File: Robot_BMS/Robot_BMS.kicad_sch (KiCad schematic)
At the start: 15 parts, among them IC1 BQ34Z100PWR-R2, IC2 STUSB4710AQTR, J1 USB_C_Receptacle_PowerOnly_24P, U1 BQ297xy, U2 BQ297xy, U3 BQ297xy, U4 MCP73833-xxx-MF, U5 MCP73833-xxx-MF, U6 MCP73833-xxx-MF

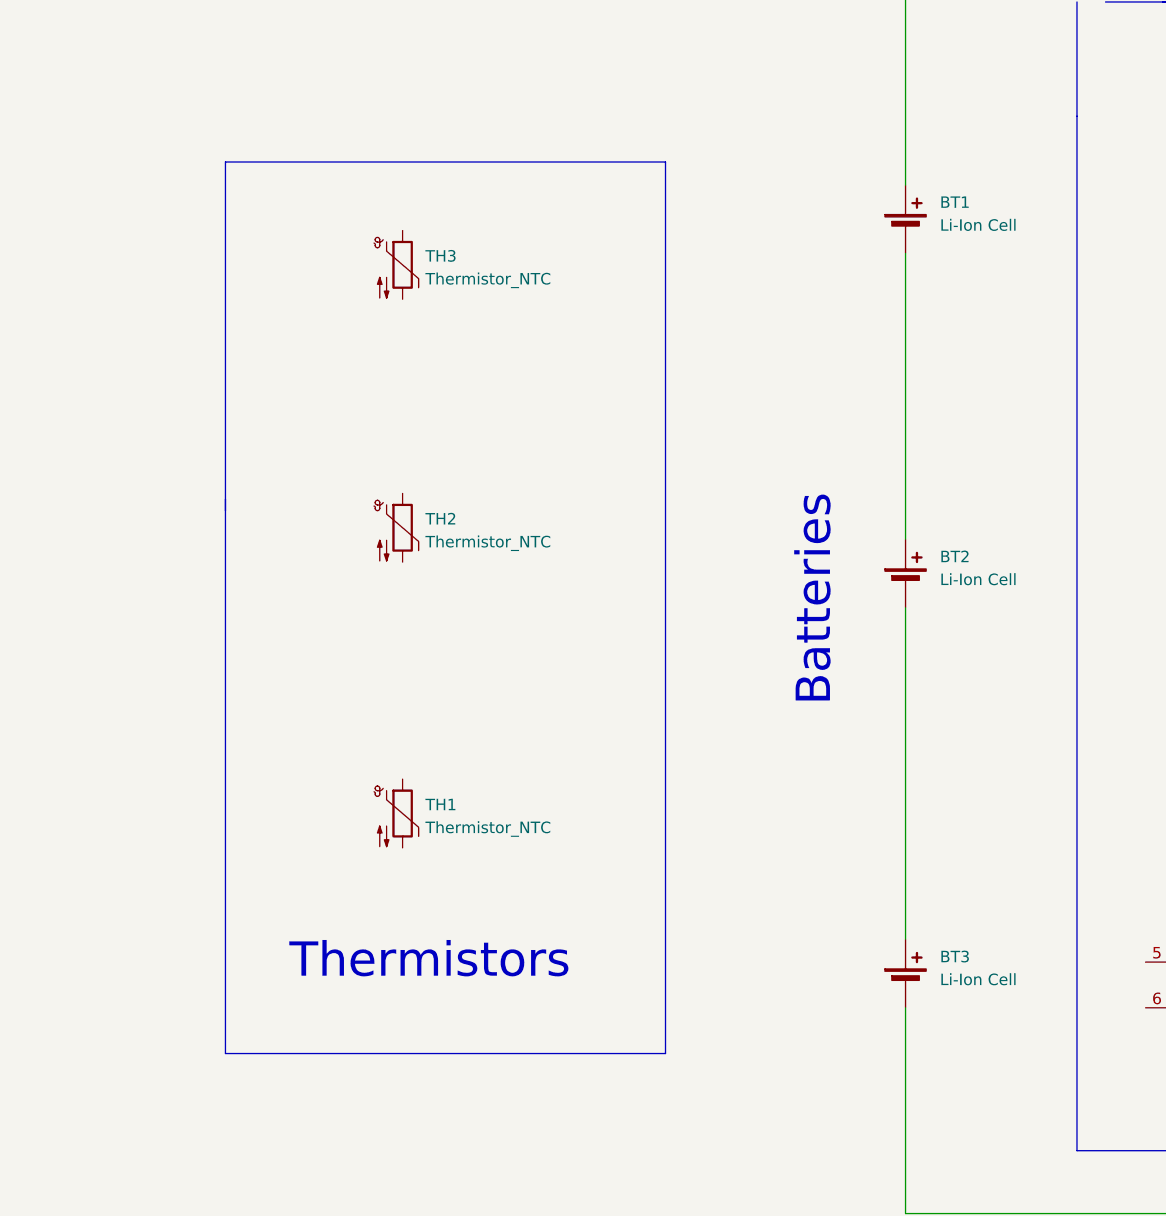
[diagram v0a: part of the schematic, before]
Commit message: NTC's implemented
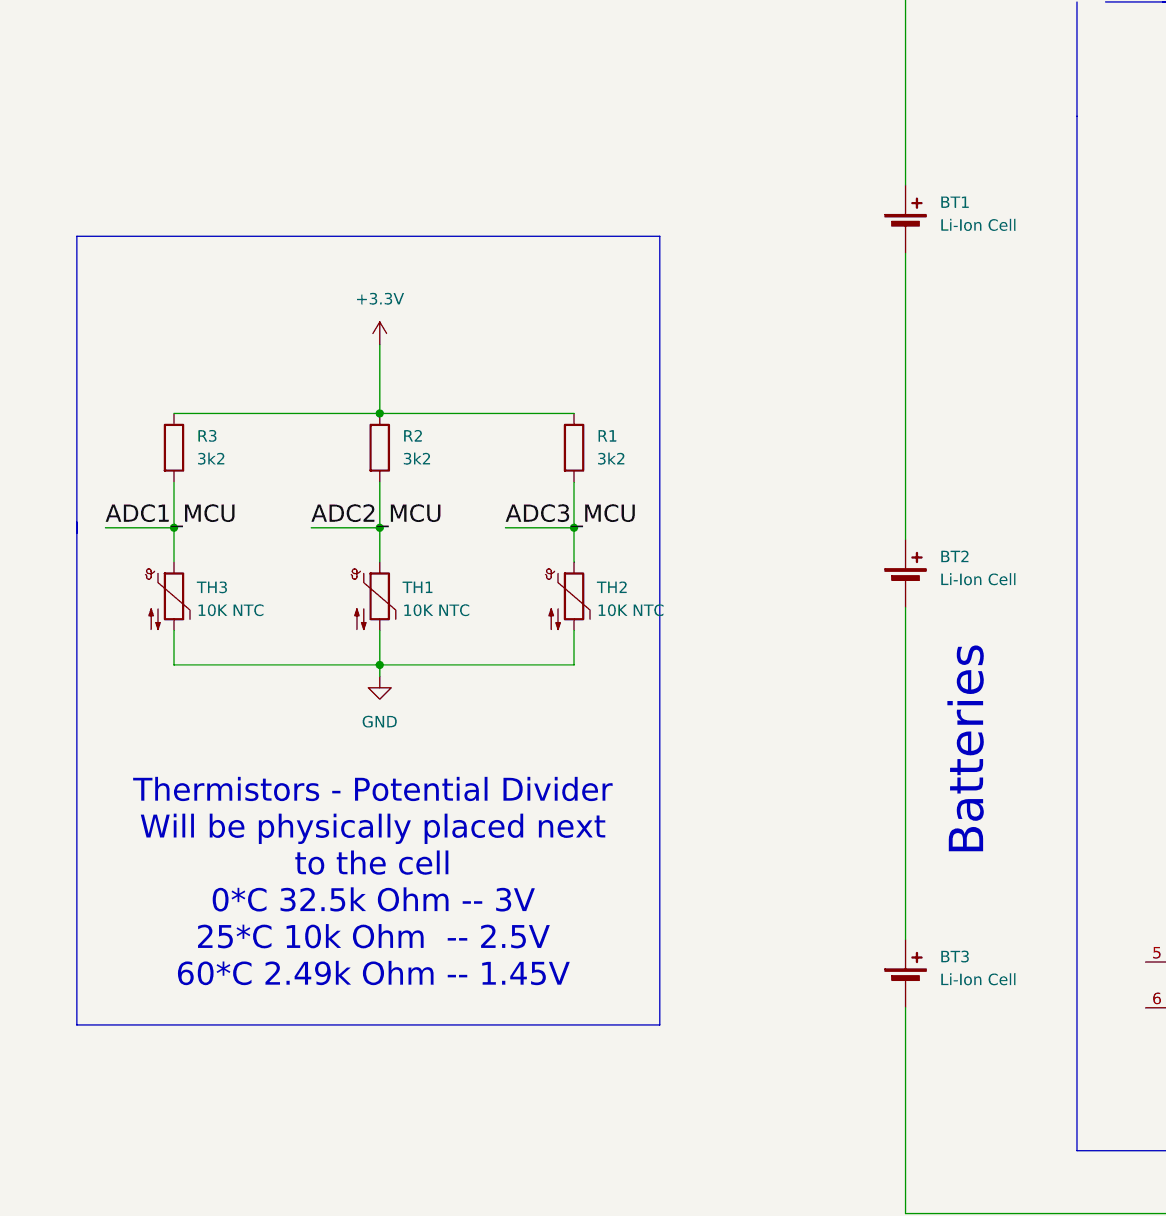
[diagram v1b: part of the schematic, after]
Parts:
- added R1, R2, R3: 3k2, symbol Device:R
- TH1, TH2, TH3: value Thermistor_NTC -> 10K NTC
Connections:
- net ADC3_MCU: now reaches TH2.1
- net ADC3_MCU: now also R1.2
- net GND: now reaches TH2.2
- net GND: now also TH1.2, TH3.2
- net ADC1_MCU: now reaches TH3.1
- net ADC1_MCU: now also R3.2
- net ADC2_MCU: now reaches TH1.1
- net ADC2_MCU: now also R2.2
- new net +3.3V: R1.1, R2.1, R3.1
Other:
- note added: "Thermistors - Potential Divider Will be physically placed next to the cell 0*C 32.5k Ohm -- 3V 25*C 10k Ohm -- 2.5V 60*C 2.49k Ohm -- 1.45V"
- note removed: "Thermistors"
- moved on the sheet: TH3

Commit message: Battery Protection IC implemented, N Channel Fet selected
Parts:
- added C1, C2, C3: 0.1u, symbol Device:C
- added Q1, Q2, Q3, Q4, Q5, Q6: SIS413DN-T1-GE3, SIS862DNT1GE3, symbol SIS413DN-T1-GE3:SIS413DN-T1-GE3
- added R4, R6, R8: 2k2, symbol Device:R
- added R5, R7, R9: 330, symbol Device:R
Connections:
- net at BT1.1 (+): now also R5.1
- net at BT1.2 (-), BT2.1 (+): now also Q2.1 (S_1), Q2.2 (S_2), Q2.3 (S_3), R7.1
- net at U2.2 (Cout): now also Q3.4 (G)
- net at U2.3 (Dout): now also Q4.4 (G)
- net at U2.4 (VSS): now also C2.2, Q4.5 (D_1), Q4.6 (D_2), Q4.7 (D_3), Q4.8 (D_4), R6.1
- net at U2.5 (BAT): now also C2.1, R7.2
- net at U2.6 (V-): now also R6.2
- net at BT2.2 (-), BT3.1 (+): now also Q3.1 (S_1), Q3.2 (S_2), Q3.3 (S_3), R9.1
- net at BT3.2 (-): now also Q5.1 (S_1), Q5.2 (S_2), Q5.3 (S_3)
- net at U1.2 (Cout): now also Q2.4 (G)
- net at U1.3 (Dout): now also Q1.4 (G)
- net at U1.4 (VSS): now also C1.2, Q1.5 (D_1), Q1.6 (D_2), Q1.7 (D_3), Q1.8 (D_4), R4.1
- net at U1.5 (BAT): now also C1.1, R5.2
- net at U1.6 (V-): now also R4.2
- net at U3.2 (Cout): now also Q5.4 (G)
- net at U3.3 (Dout): now also Q6.4 (G)
- net at U3.4 (VSS): now also C3.2, Q6.5 (D_1), Q6.6 (D_2), Q6.7 (D_3), Q6.8 (D_4), R8.1
- net at U3.5 (BAT): now also C3.1, R9.2
- net at U3.6 (V-): now also R8.2
- new net: Q5.5 (D_1), Q5.6 (D_2), Q5.7 (D_3), Q5.8 (D_4), Q6.1 (S_1), Q6.2 (S_2), Q6.3 (S_3)
- new net: Q1.1 (S_1), Q1.2 (S_2), Q1.3 (S_3), Q2.5 (D_1), Q2.6 (D_2), Q2.7 (D_3), Q2.8 (D_4)
- new net: Q3.5 (D_1), Q3.6 (D_2), Q3.7 (D_3), Q3.8 (D_4), Q4.1 (S_1), Q4.2 (S_2), Q4.3 (S_3)
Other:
- note added: "The drain current of the FET determines, charging and discharging current"
- note removed: "Batteries"
- moved on the sheet: BT1, R1, R2, R3, TH1, TH2, TH3, U1

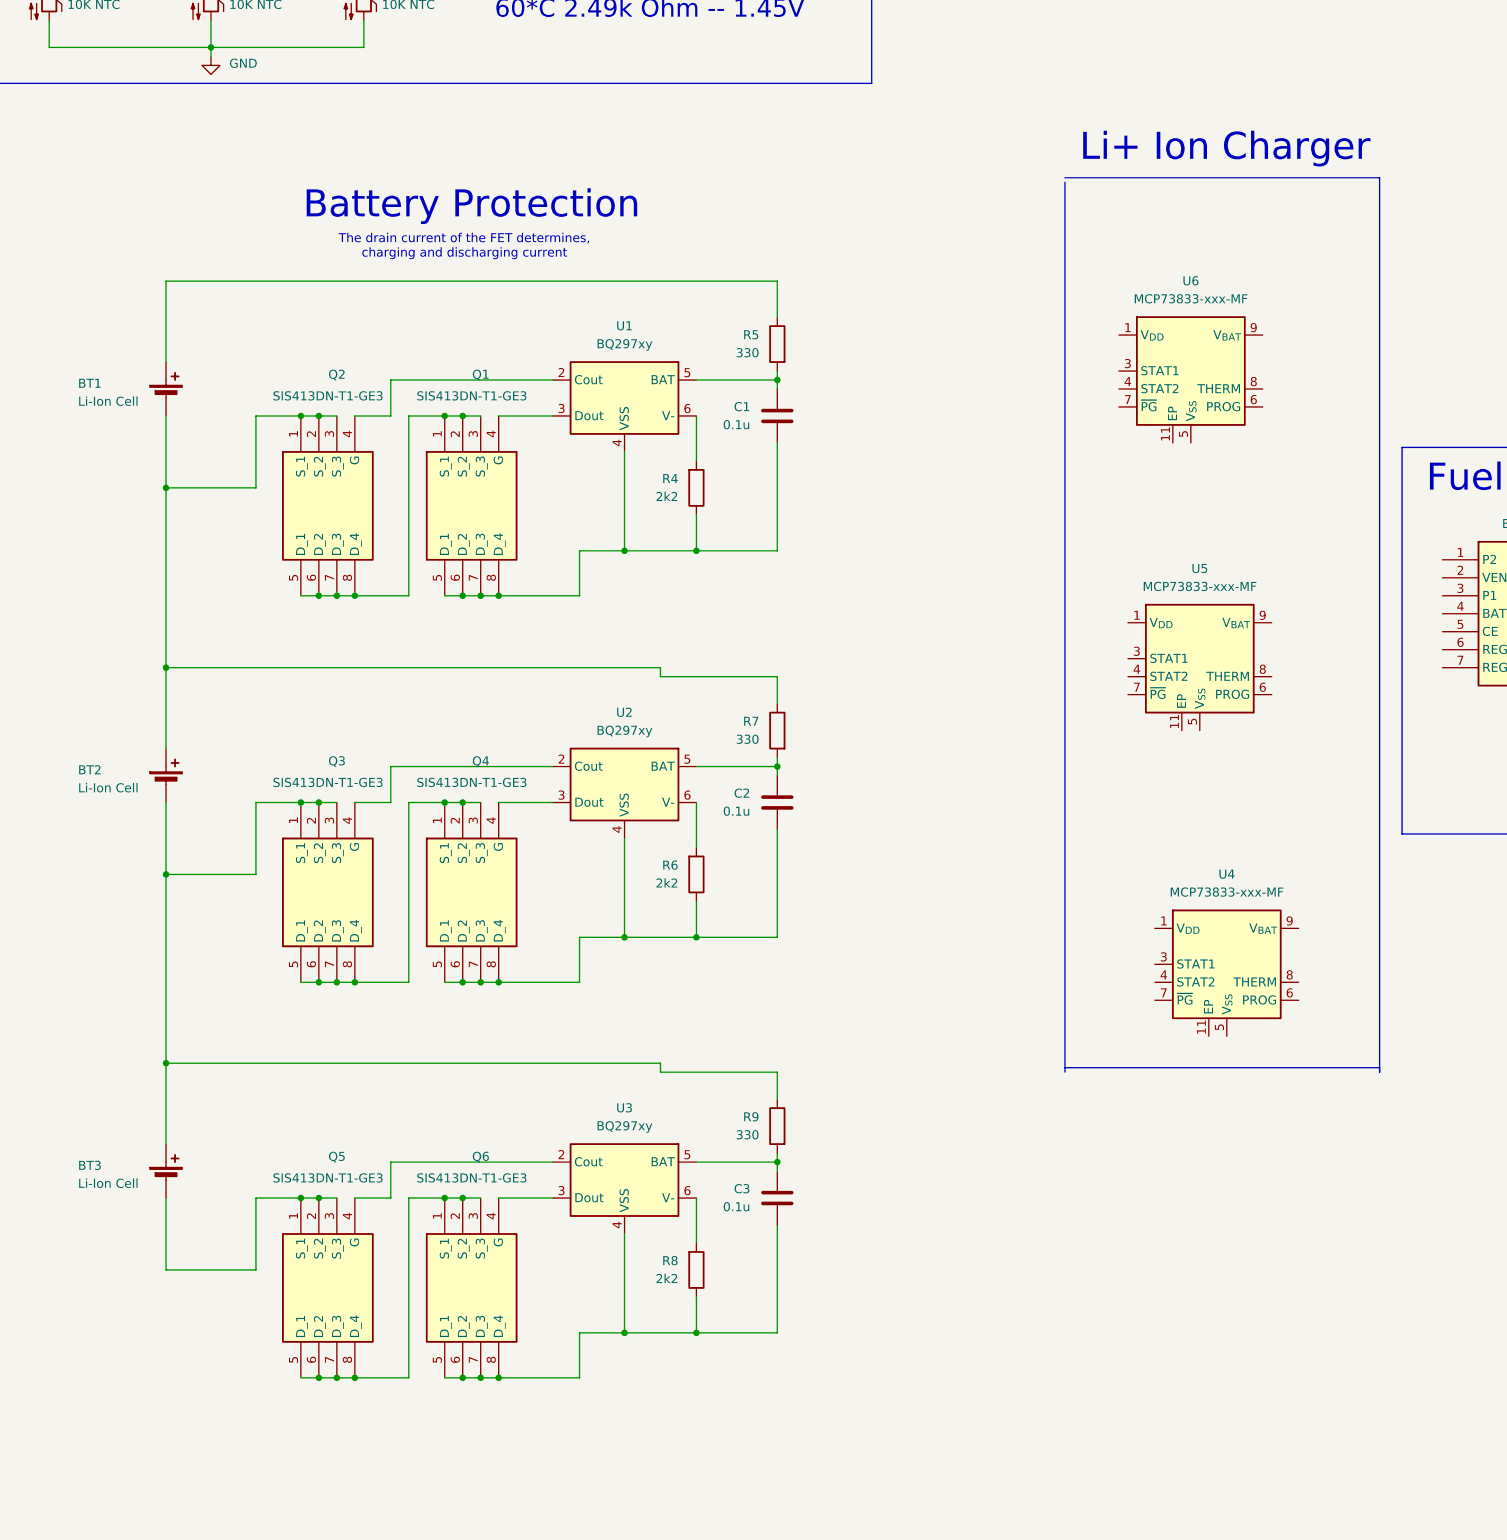
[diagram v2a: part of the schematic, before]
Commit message: comments on Bat Protection IC added
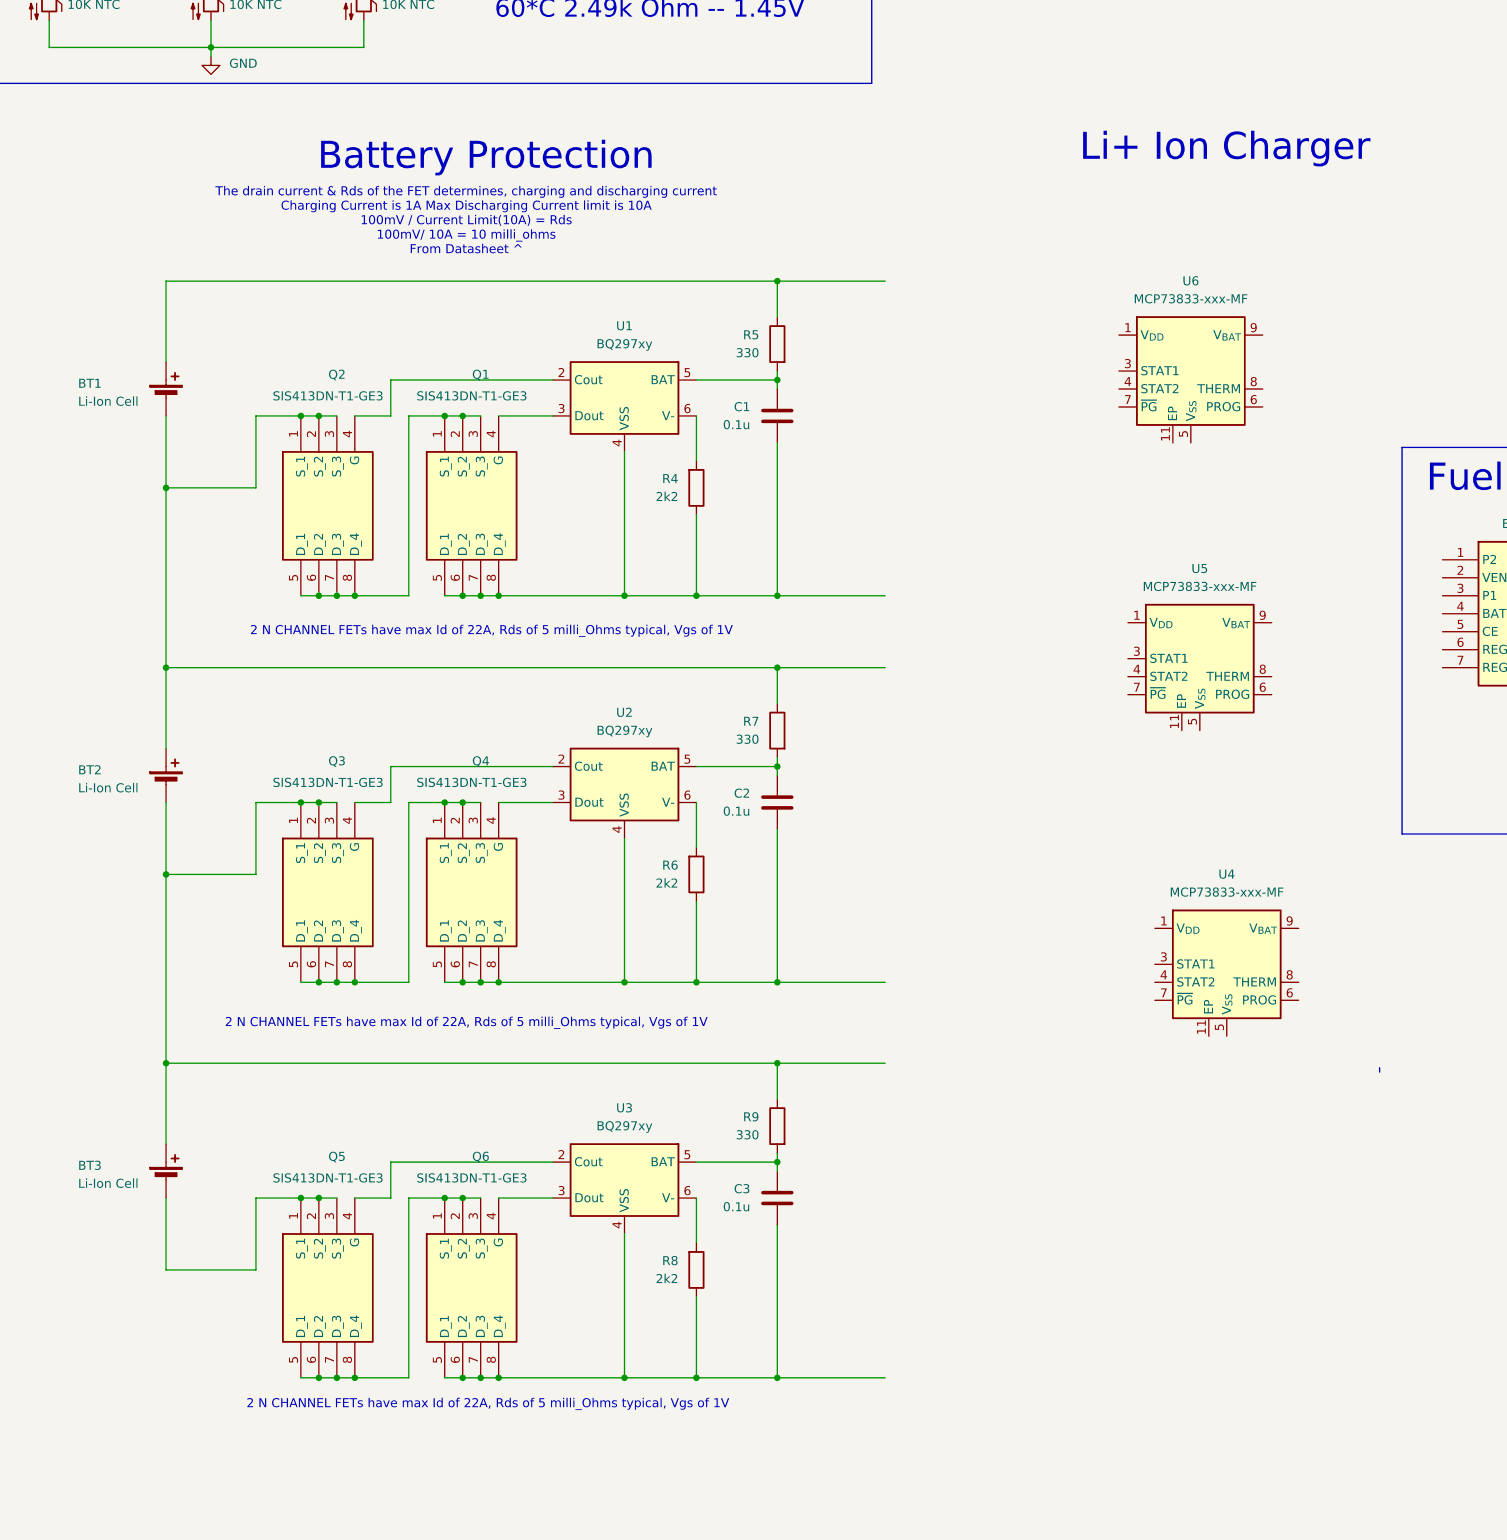
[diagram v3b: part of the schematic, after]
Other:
- note added: "2 N CHANNEL FETs have max Id of 22A, Rds of 5 milli_Ohms typical, Vgs of 1V"
- note added: "The drain current & Rds of the FET determines, charging and discharging current Charging Current is 1A Max Discharging Current limit is 10A 100mV / Current Limit(10A) = Rds 100mV/ 10A = 10 milli_ohms From Datasheet ^"
- note removed: "The drain current of the FET determines, charging and discharging current"

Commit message: Li+ Ion implemented into schematic for one of the cells
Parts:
- removed U4, U5: MCP73833-xxx-MF, Package_DFN_QFN:DFN-10-1EP_3x3mm_P0.5mm_EP1.58x2.35mm, symbol Battery_Management:MCP73833-xxx-MF
- added C4, C5: 10u, symbol Device:C
- added LED1: SML-D12V8WT86, SMLD12V8WT86, symbol SML-D12V8WT86:SML-D12V8WT86
- added LED2: KT_EELP41.12-S2U1-25-2X4X-5-R18, KTEELP4112S2U1252X4X5R18, symbol KT EELP41.12-S2U1-25-2X4X-5-R18:KT_EELP41.12-S2U1-25-2X4X-5-R18
- added LED3: KY_EELP41.22_Q2T1-36-A8J8-020-R18, KYEELP4122Q2T136A8J8020R18, symbol KY EELP41.22 Q2T1-36-A8J8-020-R18:KY_EELP41.22_Q2T1-36-A8J8-020-R18
- added Q7: 2N7002, Package_TO_SOT_SMD:SOT-23, symbol Transistor_FET:2N7002
- added R10, R11, R12: 400, symbol Device:R
- added R13: 1k, symbol Device:R
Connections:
- net at BT1.1 (+), R5.1: now also U6.10 (V_{BAT}), U6.9 (V_{BAT}), C4.1
- net at C1.2, Q1.5 (D_1), Q1.6 (D_2)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: now also U6.11 (EP), U6.5 (V_{SS}), C4.2, C5.2, Q7.2 (S)
- net at U6.1 (V_{DD}), U6.2 (V_{DD}): now also C5.1, LED1.2 (A), LED2.2 (A), LED3.2 (A)
- net at U6.3 (STAT1): now also R10.1
- net at U6.4 (STAT2): now also R11.1
- net at U6.6 (PROG): now also R13.2
- net at U6.7 (~{PG}): now also R12.1
- new net: LED3.1 (K), R12.2
- new net: LED1.1 (K), R10.2
- new net: Q7.3 (D), R13.1
- new net: LED2.1 (K), R11.2
- new net CHRG_EN: Q7.1 (G)
- no-connect marks 0 -> 1
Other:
- note added: "LED1,2,3 FWD Voltage - 2 to 2.4V FWD Current - ~7mA"
- note added: "STAT1 LED ON - Charge In Progress STAT2 LED ON - Charge Done PG(Power Good) - Low unless in shutdown mode PROG pin left floating disables charger CHRG_EN Set High to enable charging"
- moved on the sheet: C1, C2, C3, IC1, R5, R7, R9, U6

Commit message: Removed USB-C PD chip in favor of using resistors to neogitate 5V 3A (15W) charging
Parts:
- removed IC2: STUSB4710AQTR, QFN50P400X400X100-25N-D, symbol STUSB4710AQTR:STUSB4710AQTR
- added C6, C7, C8, C9: 10u, symbol Device:C
- added LED4, LED7: SML-D12V8WT86, SMLD12V8WT86, symbol SML-D12V8WT86:SML-D12V8WT86
- added LED5, LED8: KT_EELP41.12-S2U1-25-2X4X-5-R18, KTEELP4112S2U1252X4X5R18, symbol KT EELP41.12-S2U1-25-2X4X-5-R18:KT_EELP41.12-S2U1-25-2X4X-5-R18
- added LED6, LED9: KY_EELP41.22_Q2T1-36-A8J8-020-R18, KYEELP4122Q2T136A8J8020R18, symbol KY EELP41.22 Q2T1-36-A8J8-020-R18:KY_EELP41.22_Q2T1-36-A8J8-020-R18
- added Q8, Q9: 2N7002, Package_TO_SOT_SMD:SOT-23, symbol Transistor_FET:2N7002
- added R14, R18: 1k, symbol Device:R
- added R15, R16, R17, R19, R20, R21: 400, symbol Device:R
- added U4, U5: MCP73833-xxx-MF, Package_DFN_QFN:DFN-10-1EP_3x3mm_P0.5mm_EP1.58x2.35mm, symbol Battery_Management:MCP73833-xxx-MF
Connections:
- net at C3.2, Q6.5 (D_1), Q6.6 (D_2)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: now also C8.2, C9.2, Q9.2 (S), U5.11 (EP), U5.5 (V_{SS})
- net at BT1.2 (-), BT2.1 (+), Q2.1 (S_1)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: now also C6.1, U4.10 (V_{BAT}), U4.9 (V_{BAT})
- net at BT2.2 (-), BT3.1 (+), Q3.1 (S_1)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: now also C8.1, U5.10 (V_{BAT}), U5.9 (V_{BAT})
- net at C2.2, Q4.5 (D_1), Q4.6 (D_2)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: now also C6.2, C7.2, Q8.2 (S), U4.11 (EP), U4.5 (V_{SS})
- new net: LED8.1 (K), R20.2
- new net: C9.1, LED7.2 (A), LED8.2 (A), LED9.2 (A), U5.1 (V_{DD}), U5.2 (V_{DD})
- new net: LED5.1 (K), R16.2
- new net: C7.1, LED4.2 (A), LED5.2 (A), LED6.2 (A), U4.1 (V_{DD}), U4.2 (V_{DD})
- new net: Q8.3 (D), R14.1
- new net: R14.2, U4.6 (PROG)
- new net: R19.1, U5.3 (STAT1)
- new net: R20.1, U5.4 (STAT2)
- new net: R18.2, U5.6 (PROG)
- new net: R21.1, U5.7 (~{PG})
- new net: LED9.1 (K), R21.2
- new net: R17.1, U4.7 (~{PG})
- new net: LED6.1 (K), R17.2
- new net: LED7.1 (K), R19.2
- new net: LED4.1 (K), R15.2
- new net: Q9.3 (D), R18.1
- new net: R15.1, U4.3 (STAT1)
- new net: R16.1, U4.4 (STAT2)
- new net CHRG_EN_2: Q8.1 (G)
- new net CHRG_EN_3: Q9.1 (G)
- no-connect marks 1 -> 3
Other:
- note removed: "USBC-Power Delivery Chip"
- moved on the sheet: BT1, BT2, BT3, C1, C2, C3, C4, C5, IC1, LED1, LED2, LED3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
